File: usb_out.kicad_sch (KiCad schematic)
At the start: 33 parts, among them J6 USB_C_Receptacle_USB2.0, Q22 2N7002, U12 SY8105, U13 LM75B, U14 INA219AxD

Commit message: Fix footprint origins for JLC assembly
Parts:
- C70, C74, C75: LCSC C45783 -> C602037
- gave numbers to parts that had none: 2
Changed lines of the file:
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@@
       (effects (font (size 1.27 1.27)) hide)
     )
-    (property "LCSC" "C45783" (id 4) (at 53.34 69.85 0)
+    (property "LCSC" "C602037" (id 4) (at 53.34 69.85 0)
       (effects (font (size 1.27 1.27)) hide)
     )
@@
   (symbol (lib_id "Device:R_Small") (at 158.75 71.12 0) (mirror x) (unit 1)
     (in_bom yes) (on_board yes) (fields_autoplaced)
-    (property "Reference" "R?" (id 0) (at 157.2515 70.2853 0)
+    (property "Reference" "R126" (id 0) (at 157.2515 70.2853 0)
       (effects (font (size 1.27 1.27)) (justify right))
     )
@@
   (symbol (lib_id "Device:LED_Small") (at 158.75 77.47 90) (unit 1)
     (in_bom yes) (on_board yes) (fields_autoplaced)
-    (property "Reference" "D?" (id 0) (at 160.528 76.5718 90)
+    (property "Reference" "D22" (id 0) (at 160.528 76.5718 90)
       (effects (font (size 1.27 1.27)) (justify right))
     )
@@
   (symbol (lib_id "power:GND") (at 158.75 81.28 0) (unit 1)
     (in_bom yes) (on_board yes) (fields_autoplaced)
-    (property "Reference" "#PWR?" (id 0) (at 158.75 87.63 0)
+    (property "Reference" "#PWR0314" (id 0) (at 158.75 87.63 0)
       (effects (font (size 1.27 1.27)) hide)
     )
@@
       (effects (font (size 1.27 1.27)) hide)
     )
-    (property "LCSC" "C45783" (id 4) (at 106.68 69.85 0)
+    (property "LCSC" "C602037" (id 4) (at 106.68 69.85 0)
       (effects (font (size 1.27 1.27)) hide)
     )
@@
       (effects (font (size 1.27 1.27)) hide)
     )
-    (property "LCSC" "C45783" (id 4) (at 97.79 69.85 0)
-      (effects (font (size 1.27 1.27)) hide)
-    )
+    (property "LCSC" "C602037" (id 4) (at 97.79 69.85 0)
+      (effects (font (size 1.27 1.27)) hide)
+    )

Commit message: Swap GPIO2 and GPIO23 to ensure UART download mode can be entered
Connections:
- net USBFUSE: now reaches C80.1, F3.1, R81.2, R82.2
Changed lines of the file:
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@@
+    (effects (font (size 1.27 1.27)) (justify left bottom))
+  )
+  (label "USBFUSE" (at 144.78 66.04 90)
     (effects (font (size 1.27 1.27)) (justify left bottom))
   )

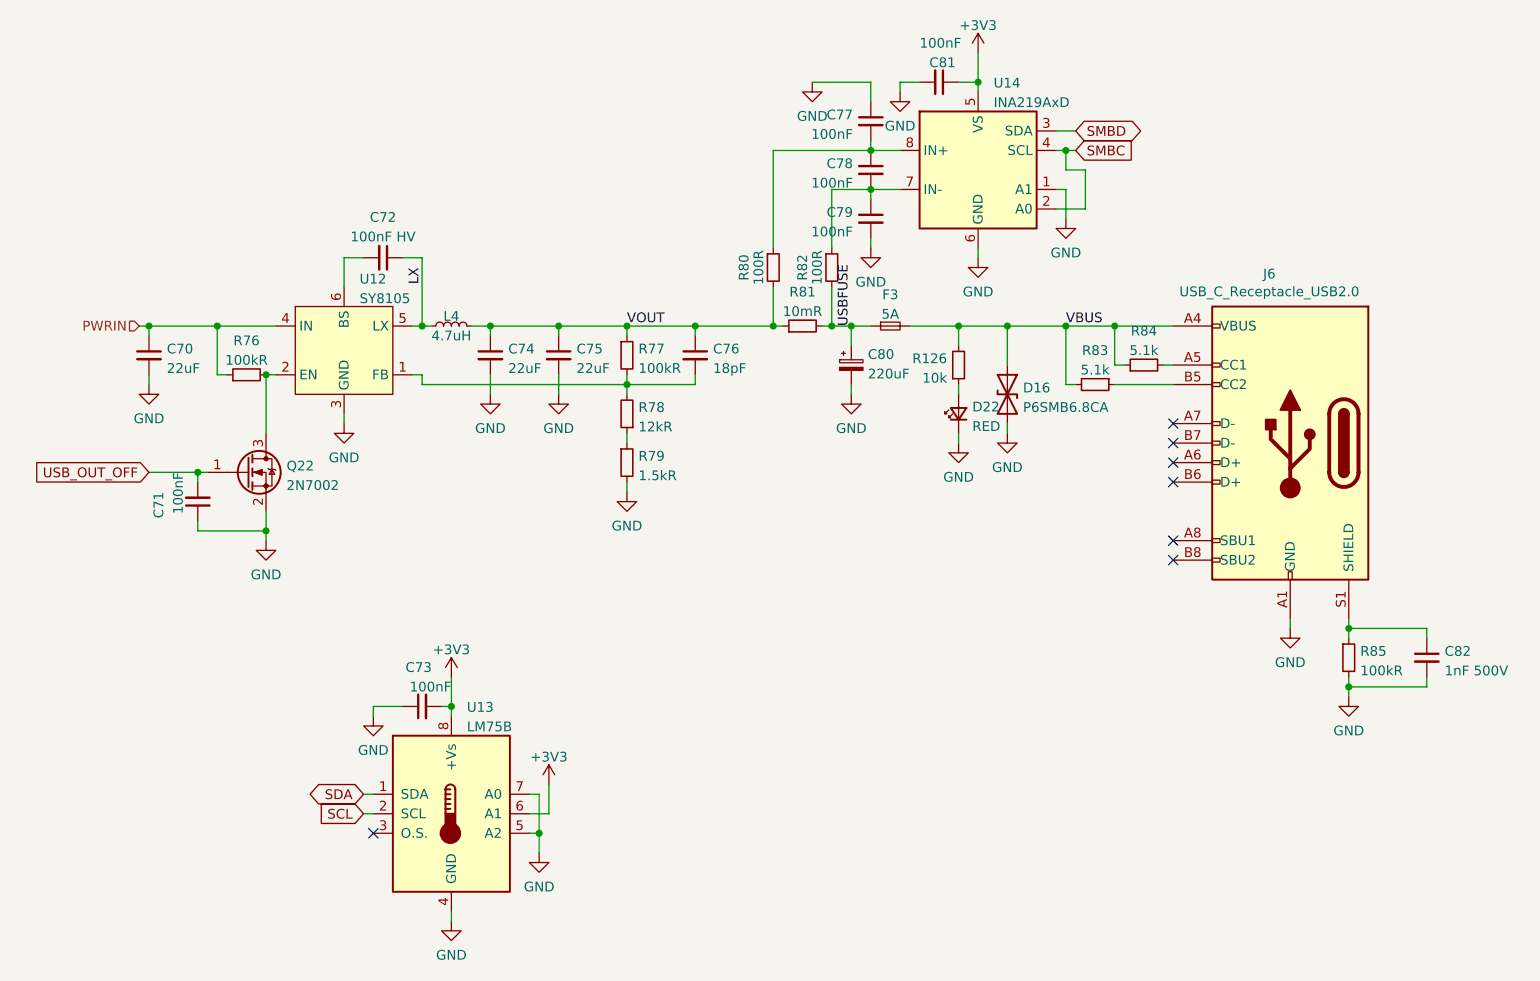
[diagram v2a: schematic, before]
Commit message: Rev 1.0 bugfixes
Changes:
 - Replace DCOK-driven DC passthrough switch with ideal diode
 - Reduce INA219 series filter resistance to 1 ohm
 - Simplify debug USB power gating
 - Fix incorrect USB CC pullups
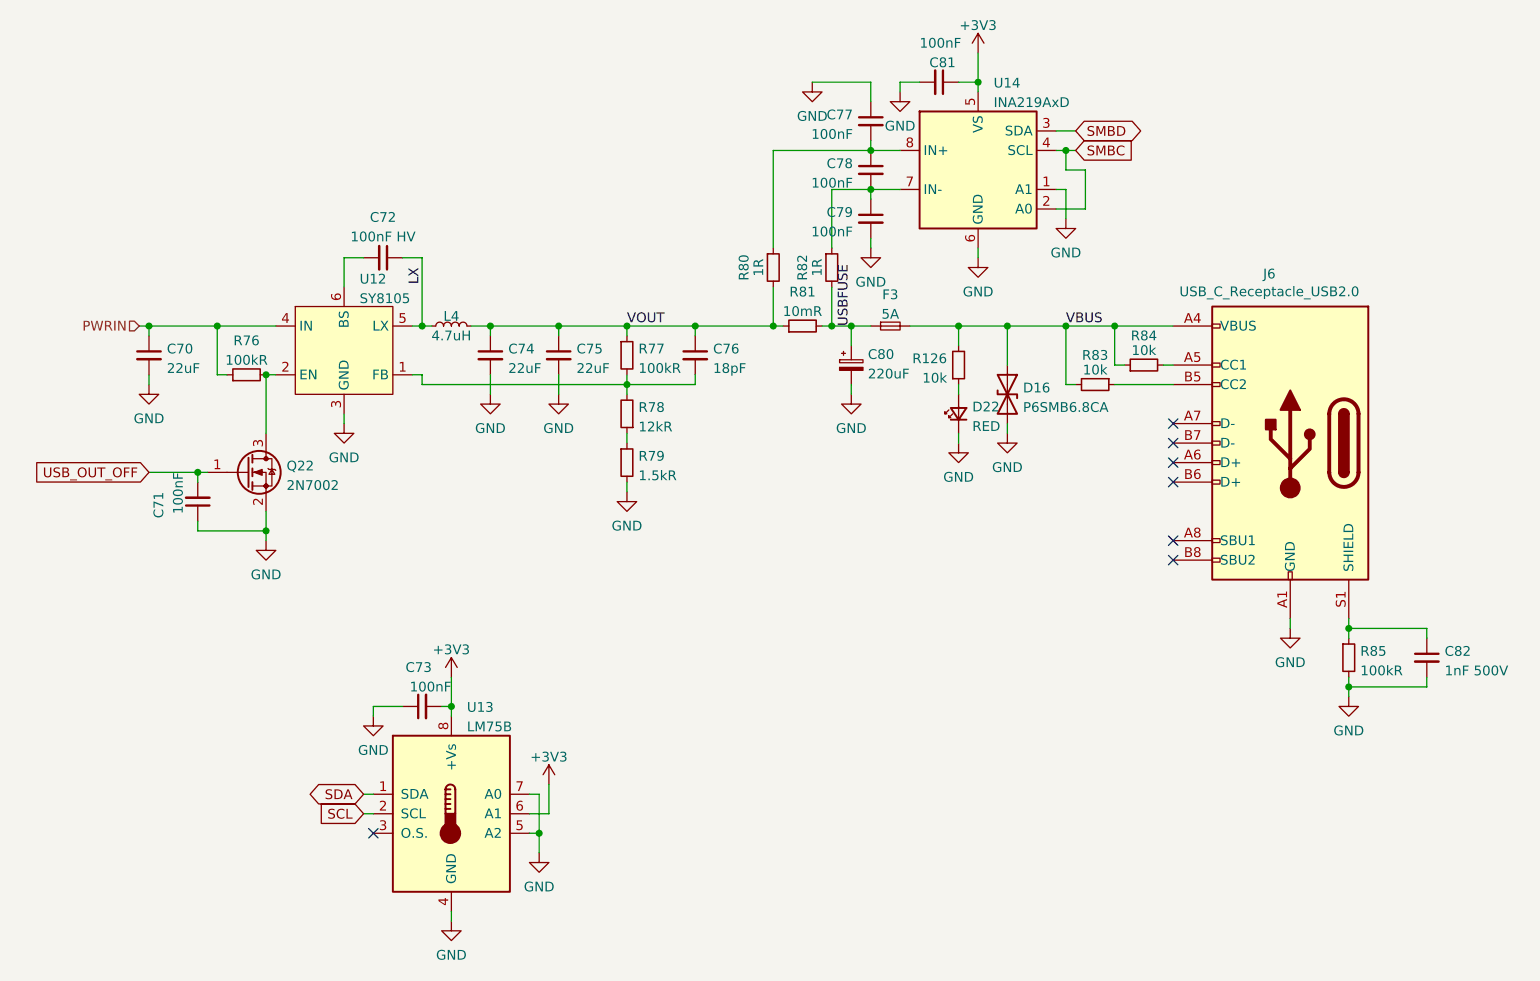
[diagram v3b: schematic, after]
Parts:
- R80, R82: value 100R -> 1R; LCSC C25076 -> C25086
- R83, R84: value 5.1k -> 10k; LCSC C25905 -> C25744
